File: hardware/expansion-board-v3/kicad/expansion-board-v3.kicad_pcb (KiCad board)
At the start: 6 copper layers, 100 x 62 mm, 156 parts, among them J1 PinHeader_2x20_P2.54mm_Vertic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, J2 U.FL_Hirose_U.FL-R-SMT-1_Vert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, J4 USB_C_Receptacle_HRO_TYPE-C-3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, J5 U.FL_Hirose_U.FL-R-SMT-1_Vert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, J6 U.FL_Hirose_U.FL-R-SMT-1_Vert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, J8 U.FL_Hirose_U.FL-R-SMT-1_Vert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, Q2 SOT-23, Q3 SOT-23, Q4 SOT-23, Q5 SOT-23, SW1 SolderJumper-2_P1.3mm_Open_Pa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, SW2 SolderJumper-2_P1.3mm_Open_Pa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, U1 SOT-23-5, U10 QFN-48-1EP_7x7mm_P0.5mm_EP5.1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, U11 DFN-8-1EP_2x2mm_P0.5mm_EP0.86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, U12 SOT-363_SC-70-6, U13 AD8319_LFCSP-8-EP, U14 MSOP-8_3x3mm_P0.65mm, U15 SOT-23-6, U16 SOT-363_SC-70-6, U17 SOT-363_SC-70-6, U2 SOT-23-5, U3 SOT-23-5, U4 BNO085_LGA-28, U5 BMP388_LGA-10, U6 LGA-16_3x3mm_P0.5mm, U7 ATGM336H_LCC-18, U8 QFN-56-1EP_7x7mm_P0.4mm_EP3.2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, U9 SOIC-8_5.3x5.3mm_P1.27mm, Y1 Crystal_SMD_3225-4Pin_3.2x2.5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, Y2 Crystal_SMD_3225-4Pin_3.2x2.5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, Y3 Crystal_SMD_3215-2Pin_3.2x1.5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

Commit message: fix(hw): D2/D3 补阴极标记线，版本号 V3.3 → V3.4
手工贴片前查极性时发现的最后一个坑：D2/D3 是 0402 封装的 ESD 管，KiCad 官方
封装 D_0402_1005Metric 只给了个**半径 0.05mm 的圆点**标 pin1，配 0.1mm 线宽，
实物可见直径约 0.2mm。这尺寸在放大镜下都难认，而它俩混在 22 个 0402 电容和
9 个 0402 电感中间外观几乎一样——贴反了电路直接不工作。

改成阴极侧一条 0.7mm 长、0.2mm 宽的标记线，比原来醒目一个数量级。
D1 是 SOD-123，官方封装的 [ 形阴极标记已经够大，不动。

方向是按电路复核过的，不是照搬 KiCad 的 pad1=阴极约定：
  D1  pad1=VCC_5V(K)/pad2=USB_VBUS(A)   USB 5V 经肖特基流向 VCC_5V，防倒灌 ✓
  D2  pad1=ANT1090_EXT(K)/pad2=GND(A)   ESD 阴极接信号、阳极接地 ✓
  D3  pad1=ANT_978(K)/pad2=GND(A)       同上 ✓

顺带删掉官方封装那个小圆点——它正好落在新标记线正中央，不删 silk_overlap
会从 1 涨到 3。挪开躲它也不行：0402 焊盘外侧就那么点地方，挪远了顶到别的
元件。删完 DRC 回到基线（未连通 0 / 铜层 0 / 丝印 2+1）。

## 修了一个更要命的隐患

排查副本重建失败时挖出来的：gen_pcb.py 读的 build/expansion.net.xml **没有
任何脚本负责刷新**，只有它读、没人写，全靠人记得手动导。实际那份停留在
11 天前，目录改名成 v3 后里面的封装库名还是旧的 "expansion-board-v3.1:"。

后果不是报错那么简单——KiCad 在库目录不存在时 FootprintLoad 返回 None，
抛的是 "NoneType object has no attribute FootprintLoad"，完全看不出根因是
网表陈旧。更坏的情况是网表只旧一点点（比如少个元件），那就会**静默**按
过时数据重建整块板。

现在 gen_pcb.py 会比对网表和原理图的 mtime，旧了就自动重导。

## 验证

  幂等          重复跑清 2 加 2，不叠加
  DRC           未连通 0 / 铜层 0 / 丝印与改动前完全一致
  从零重建       副本上 gen_pcb + gen_polarity_marks，标记坐标与主板逐个一致
  已进 rebuild.sh，重建不会丢

版本号按规则 +0.1：V3.3 的 Gerber 已经生成过，不升号会出现同一版本号对应
两份不同 Gerber。实物板仍是 V3.2，ASSEMBLY/CHECKLIST 里的首批板丝印错位
警告不受影响。
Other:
- board text added: "V3.4 2026-08"
- board text removed: "V3.3 2026-08"
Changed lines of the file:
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@@
 		(attr smd)
 		(duplicate_pad_numbers_are_jumpers no)
-		(fp_circle
-			(center -1.09 0)
-			(end -1.04 0)
-			(stroke
-				(width 0.1)
-				(type solid)
-			)
-			(fill no)
-			(layer "F.SilkS")
-		)
 		(fp_rect
 			(start -0.93 -0.47)
@@
 		(attr smd)
 		(duplicate_pad_numbers_are_jumpers no)
-		(fp_circle
-			(center -1.09 0)
-			(end -1.04 0)
-			(stroke
-				(width 0.1)
-				(type solid)
-			)
-			(fill no)
-			(layer "F.SilkS")
-		)
 		(fp_rect
 			(start -0.93 -0.47)
@@
 	)
 	(gr_line
+		(start 127.21 62.45)
+		(end 127.21 61.75)
+		(stroke
+			(width 0.2)
+			(type default)
+		)
+		(layer "F.SilkS")
+	)
+	(gr_line
+		(start 139.625 85.845)
+		(end 140.325 85.845)
+		(stroke
+			(width 0.2)
+			(type default)
+		)
+		(layer "F.SilkS")
+	)
+	(gr_line
 		(start 50 50)
 		(end 150 50)
@@
 		)
 	)
-	(gr_text "V3.3   2026-08"
+	(gr_text "V3.4   2026-08"
 		(at 100 80 0)
 		(layer "B.SilkS")

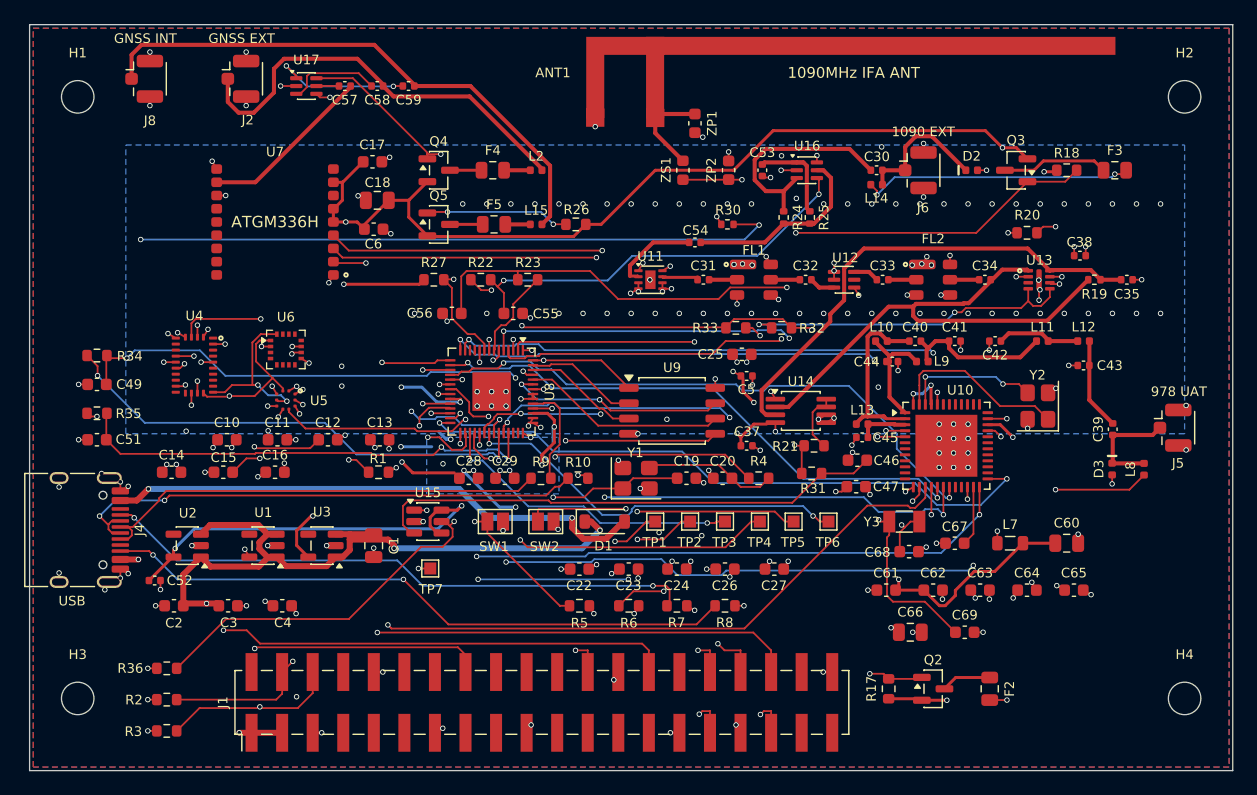
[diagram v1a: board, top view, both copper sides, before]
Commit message: fix(hw): IFA 馈线两侧挖无铜走廊，否则 0.15mm 线宽的前提不成立
0.15mm 是按**纯微带**算的（嘉立创 JLC06161H-3313 官方计算器 0.1509mm→50Ω，
参考面是 In1 完整地平面）。纯微带的前提是两侧没有近距离共面地，而板上 GND
铺铜的 zone clearance 只有 0.15mm——走线两侧 0.15mm 就是铜，实物是共面波导
不是微带，和设计模型不是一回事。天线那边刚因为「腿被 GND 包围」栽过一次。

走廊沿走线生成 keepout：半宽 = 半线宽 + 0.5mm，0.5mm ≈ 5 倍介质厚
（L1-L2 prepreg 3313 单张 0.0994mm），微带边缘场大约 3 倍介质厚内衰减完。
逐点扫描验证：两侧 ±0.20/0.35/0.50mm 命中铜 0 处，外侧 0.75mm 仍有铜
（只挖走廊没挖过头），ZP1.2 接地脚照常在铜里。

三个边界条件：
· **只挖 F.Cu**。In1 是这条微带的参考地平面，挖了不是更干净，是把传输线拆了
· **禁过孔**。只挡铺铜的话 route_rf 的 GND 缝合孔照样能打进来，一个 0.3mm
  接地过孔落在 50Ω 线旁 0.2mm 处比铺铜更糟——那是集中接地点，直接阻抗突变
· **不禁焊盘**。走廊两端压着 ZP1.1/ZS1.1 两个射频焊盘，禁了 DRC 立刻报违例

同时修 route_ifa_feed.py 一个自伤 bug：它删掉 ANT1090_IFA 的**所有**走线，
却只重布 ANT1→ZP1 一段，ZP1→ZS1 被删了没补（上一轮是拿 /tmp 里的临时脚本
手工补的，跑一次 run_route.sh 就又没了）。删多少补多少。

板子按固化后的布局从零重跑到第②"步：过孔全部重新放置（QFN 扇出环 + 60 栅栏
+ 183 缝合 + 35 EP 散热 = 313）。数字段走线仍为零，等 freerouting 指令。
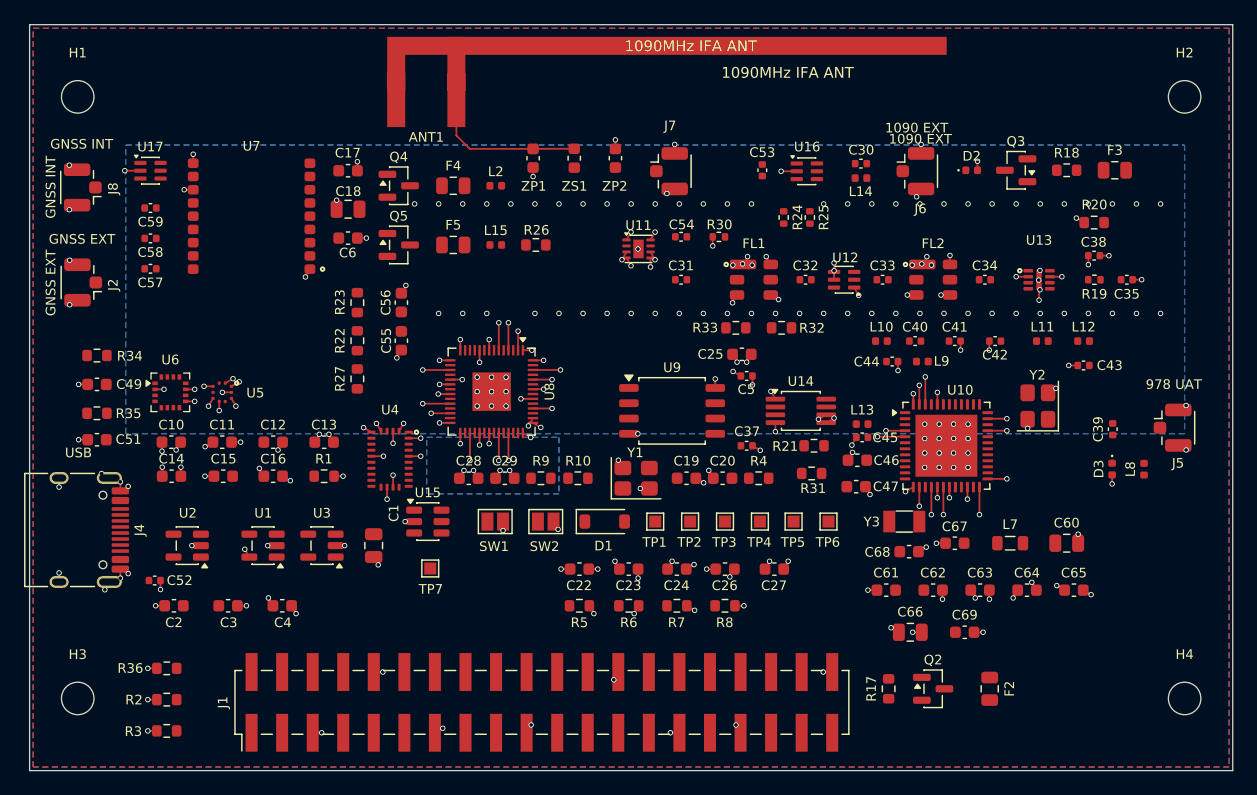
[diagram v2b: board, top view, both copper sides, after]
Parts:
- added J7: U.FL_Hirose_U.FL-R-SMT-1_Vertical, U.FL_Hirose_U.FL-R-SMT-1_Vertical, F.Cu at (103.6, 62.2)
- moved C59 23.7 mm to (60.0, 65.2), turned to 0 degrees
- moved C58 22.7 mm to (60.0, 67.8)
- moved C57 22.2 mm to (60.0, 70.3)
- moved J2 22.0 mm to (54.0, 71.4), turned to 180 degrees
- moved U4 18.0 mm to (80.0, 86.1)
- moved ANT1 16.5 mm to (85.5, 57.8)
- moved U17 14.7 mm to (60.0, 62.1)
- moved R23 14.3 mm to (77.2, 73.1), turned to -90 degrees
- moved ZP1 13.8 mm to (91.8, 61.1)
- moved R22 11.4 mm to (77.2, 76.3), turned to 90 degrees
- moved J8 10.9 mm to (54.0, 63.5), turned to 180 degrees
- moved R27 10.4 mm to (77.2, 79.4), turned to 90 degrees
- moved U6 10.2 mm to (61.7, 80.6)
- moved C55 9.57 mm to (80.9, 76.3), turned to -90 degrees
- moved ZP2 9.46 mm to (98.7, 61.1)
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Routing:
- net 3V3_GNSS: track 169.6 -> 0.00 mm, vias 6 -> 0
- net RF_DET_OUT: track 122.3 -> 0.00 mm, vias 6 -> 0
- net SUBG_MISO: track 78.2 -> 0.89 mm, vias 2 -> 1
- net VCC_5V: track 74.4 -> 0.00 mm, vias 4 -> 0
- net LEVEL_BIAS: track 72.1 -> 0.00 mm, vias 5 -> 0
- net GNSS_TXD: track 69.0 -> 0.00 mm, vias 2 -> 0
- net SLICER_LEVEL: track 66.5 -> 0.00 mm, vias 4 -> 0
- net SUBG_RESET: track 67.1 -> 2.48 mm, vias 4 -> 2
- net GNSS_PPS: track 63.4 -> 0.00 mm, vias 2 -> 0
- net SUBG_TMSC: track 63.7 -> 2.29 mm, vias 3 -> 1
- net GNSS_RXD: track 61.1 -> 0.00 mm, vias 2 -> 0
- net BIAS_EN_978: track 60.9 -> 0.00 mm, vias 3 -> 0
- net 3V3_RF: track 66.8 -> 6.25 mm, vias 16 -> 8
- net IMU_INT: track 60.4 -> 0.00 mm, vias 2 -> 0
- net BIAS_EN_1090: track 58.7 -> 2.29 mm, vias 2 -> 1
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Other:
- board text added: "V3.5 2026-08"
- board text removed: "3V3-D"
- board text removed: "3V3-G"
- board text removed: "3V3-RF"
- board text removed: "AD8313"
- board text removed: "AD8319"
- board text removed: "ATGM336H"
- board text removed: "BMP388"
- board text removed: "BNO085"
- board text removed: "CC1312R"
- board text removed: "LNA1"
- board text removed: "LNA2"
- board text removed: "QMC5883"
- board text removed: "RP2040"
- board text removed: "SW1090"
- board text removed: "SWGNSS"
- board text removed: "TLV3501"
- board text removed: "V3.4 2026-08"
- board text removed: "W25Q128"

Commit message: chore(hw): 按固化布局重建板子，J7 标注 + 无铜走廊 + 45° 扇出全部落盘
板子重跑到第②"步并补齐第⑦/⑦'步：309 走线 / 313 过孔（QFN 扇出环 + 60 栅栏
+ 183 缝合 + 35 EP 散热，全部重新放置）。板级文字 12 条无重复，'1090 IFA'
已在板上，位号字高 0.8mm。

DRC 只剩 via_dangling 35（数字段未布线，缝合孔暂时悬空，布通后自然消）
和 silk_edge_clearance 2（既存）。silk_overlap 归零。

数字段仍未布线：freerouting 卡在 45° 后处理不出 SES，四种组合全试过都一样，
见下一条提交里的记录。
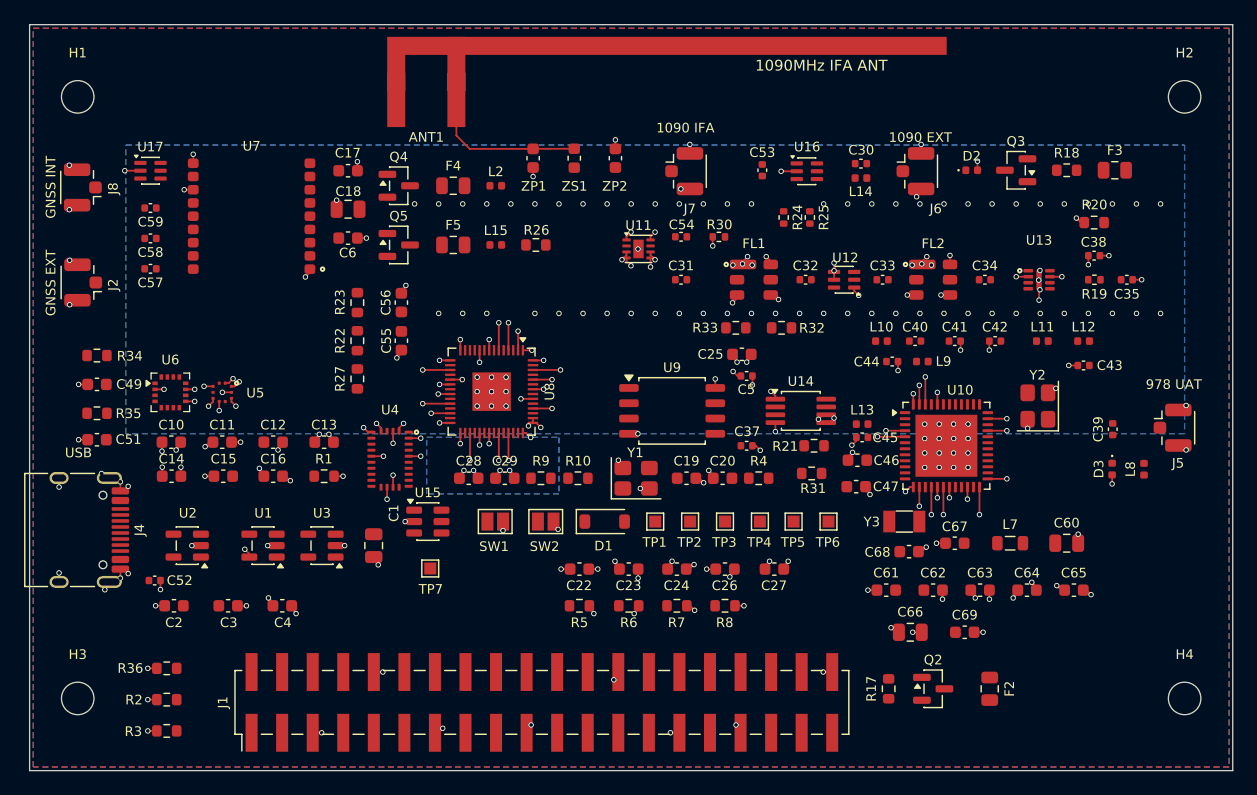
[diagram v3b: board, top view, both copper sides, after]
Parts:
- moved J7 1.26 mm to (104.9, 62.2)
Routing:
- net GND: track 100.6 -> 103.8 mm
- net 3V3_DIG: track 34.8 -> 35.9 mm
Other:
- board text added: "1090 IFA"

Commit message: feat(hw): 改用 KRT 布数字段，未连通 207 → 55
freerouting 布得完但吐不出 SES（六种组合全试过，见上一条提交）。换 KRT——
KiCadRoutingTools 0.19.1，Rust A*，装在 KiCad 10 的 3rdparty 插件目录里。
上一条记忆写着「KRT 已经找不回来了」，是错的，它一直在。

它直接读写 .kicad_pcb，不走 DSN/SES，freerouting 那个坑整个绕开；而且是
octilinear（H/V/45°），天然没有会卡死的 45 度化后处理。布线本体只花 17 秒。

结果：走线 309→1864（F.Cu 1688 / B.Cu 85 / In2.Cu 91），过孔 437，
真缺线 207→55。铜层 DRC 只剩 starved_thermal 2 + track_dangling 1。
射频 258 段全在 F.Cu、线宽 0.15、零过孔，In1 参考面完整；
IFA 馈线四段一字未动，无铜走廊仍在，馈线两侧和天线两脚 0 处命中铜。

## 四个坑，都踩了

1. **它不重新填充覆铜。** 新走线/过孔穿过旧的填充铜，DRC 报 clearance 505 +
   hole_clearance 200，看着像布线质量差。跑一次 ZONE_FILLER 之后 505→33、200→0
   ——而 Track↔Track 自始至终只有 4 条。判据：先看违例的参与者类型，带 Zone 的
   先去填铜再下结论。

2. **per-netclass 规则要显式给。** --clearance 一旦显式传就会覆盖它从 sibling
   .kicad_pro 自动读的 per-netclass 值。第一轮传了 0.15，POWER 类（要求 0.2、
   线宽 0.5）被按 Default 布成 0.15——93 条通但 33 条 clearance 违例，而且
   USB_VBUS/VCC_5V 用 0.15mm 载流根本不够。改用 --power-nets + --power-nets-widths
   之后 80 条通、clearance 归零。少通 13 条是真实代价，不是退步。

3. **reconciliation 阶段不看 --nets 过滤。** 我排除了全部 27 个 RF50 网络，
   它的 kicad-oracle reconnect 照着 KiCad DRC 的未连通表把 7 条射频布到了
   B.Cu/In2.Cu 上，打了 18 个过孔——那是在 50Ω 线的参考面上开洞。事后清掉，
   再迭代 clean_dangling 收敛。

4. **它会偷改 .kicad_pro**（这次 26 项），老毛病。在 build/krt/ 副本里跑，
   只回拷 .kicad_pcb。

另外它放了 3 个 0.25/0.15 的过孔（板规要求直径 ≥0.3、环宽 ≥0.07）。改 0.45 会撞
邻居，改 0.30/0.15 正好：直径等于下限、环宽 0.075>0.07，两项都过。

剩余 55 条真缺线里 3V3_GNSS 独占 14 条——它没有覆铜平面（可缝合网络只有
3V3_DIG/3V3_RF/GND/RP_1V1），却被我当平面网排除掉了，下一轮不该排除它。
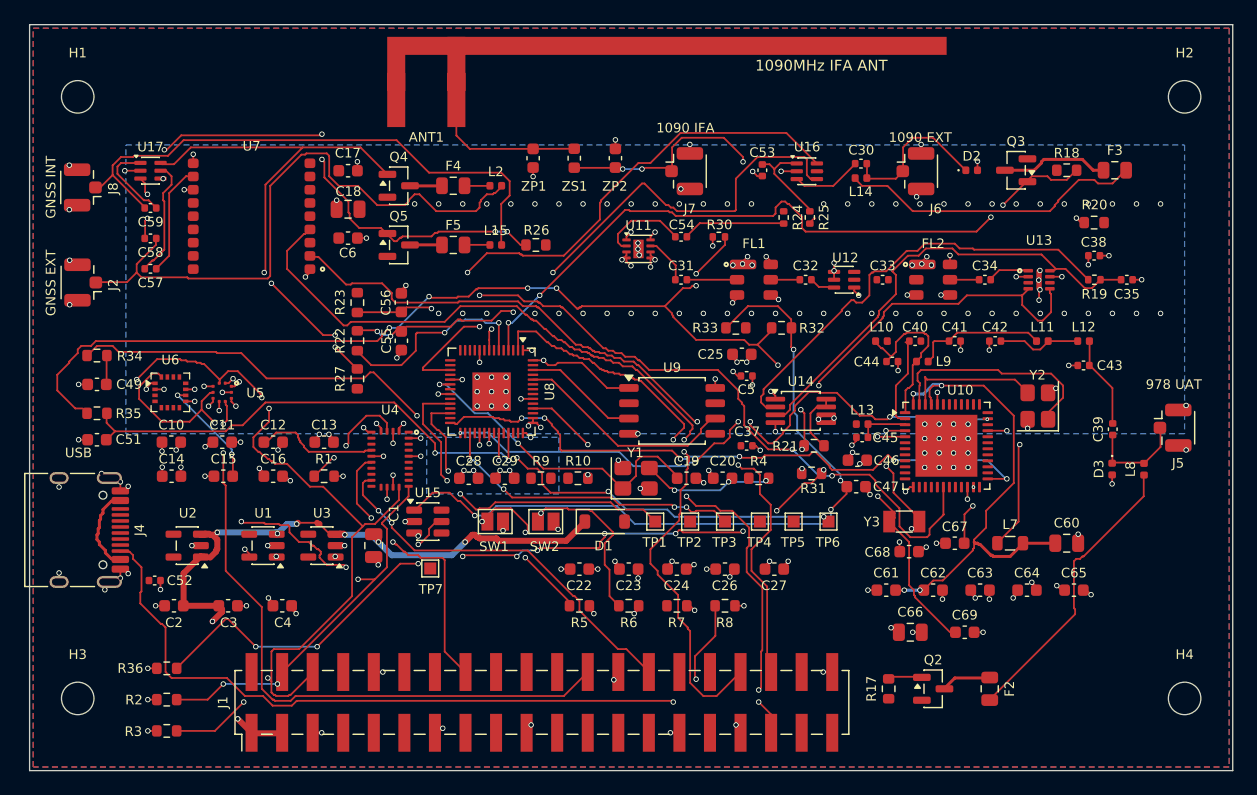
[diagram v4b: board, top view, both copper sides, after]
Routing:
- net RF_DET_OUT: track 0.00 -> 119.3 mm, vias 0 -> 11
- net GNSS_PPS: track 0.00 -> 74.6 mm, vias 0 -> 2
- net I2C_SCL: track 0.00 -> 69.8 mm, vias 0 -> 6
- net I2C_SDA: track 0.00 -> 66.6 mm, vias 0 -> 6
- net VCC_5V: track 0.00 -> 66.5 mm, vias 0 -> 10
- net USB_CC2: track 0.00 -> 65.4 mm, vias 0 -> 2
- net GNSS_TXD: track 0.00 -> 63.6 mm, vias 0 -> 2
- net SLICER_LEVEL: track 0.00 -> 62.9 mm, vias 0 -> 4
- net SUBG_IRQ: track 4.58 -> 64.0 mm, vias 2 -> 4
- net BIAS_EN_1090: track 2.29 -> 58.4 mm, vias 1 -> 4
- net BARO_INT: track 0.00 -> 53.9 mm, vias 0 -> 2
- net ANT_GNSS_EXT: track 0.00 -> 51.5 mm
- net SUBG_TCKC: track 2.48 -> 52.9 mm, vias 2 -> 6
- net ANT_SEL_GNSS_A: track 0.89 -> 50.7 mm, vias 1 -> 7
- net ANT_SEL_1090_V1: track 0.00 -> 49.3 mm, vias 0 -> 4
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
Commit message: feat(hw): KRT 收尾脚本化，真缺线 55 → 41（3V3_GNSS 那 14 条清零）
上一轮把 3V3_GNSS 当"平面网"排除掉了，可它**根本没有覆铜平面**——板上真有
覆铜的只有 GND / 3V3_DIG / 3V3_RF / RP_1V1。它需要走线连接却被挡在门外，
55 条真缺线里一家独占 14 条。这一轮放开，14 条清零。

根治办法不是把名单改对，是**不再写死名单**：krt_post.py 的 nets 模式直接从板上
的覆铜区读，板子怎么变名单就怎么变。POWER/POWER_LO 的线宽同样从 .kicad_pro 的
netclass 读，并自动跳过已有平面和已布好的射频。

新增 tools/krt_post.py，把 KRT 的收尾固化成一条命令（手工来一遍必漏）：

    ① 清射频越层  —— 它的 reconciliation 阶段不看 --nets 过滤，会照着 KiCad DRC
                     的未连通表把射频布到 B.Cu/In2.Cu 并打过孔，那是在 50Ω 线的
                     参考面上开洞
    ② 修不合规过孔 —— 实测它放过 0.25/0.15；改 0.45 会撞邻居，0.30/0.15 正好
                     （直径等于下限、环宽 0.075>0.07）
    ③ 覆铜重填    —— 它不填。不填的话新走线穿过旧填充铜，DRC 报 clearance 505 +
                     hole_clearance 200，看着像布线烂，其实全是 Track/Via↔Zone
    ④ 断头铜迭代  —— 删过孔会露出新的断头走线，一轮清不完，清到收敛为止

本轮结果：走线 1997 段（F.Cu 1806 / B.Cu 94 / In2.Cu 97），过孔 451，
真缺线 41 处 / 31 网络，铜层 DRC 3 条（starved_thermal 2 + track_dangling 1）。
射频 257 段全在 F.Cu、线宽 0.15、零过孔；IFA 馈线 4 段完好，走廊仍禁铺铜禁过孔，
馈线两侧和天线两脚 0 处命中铜；板级文字 12 条无重复。

剩下 41 条分散在 31 个网络（QSPI/SUBG/USB 各 1-5 条），已是硬骨头，
再压要靠 rip-up reroute 或改布局。
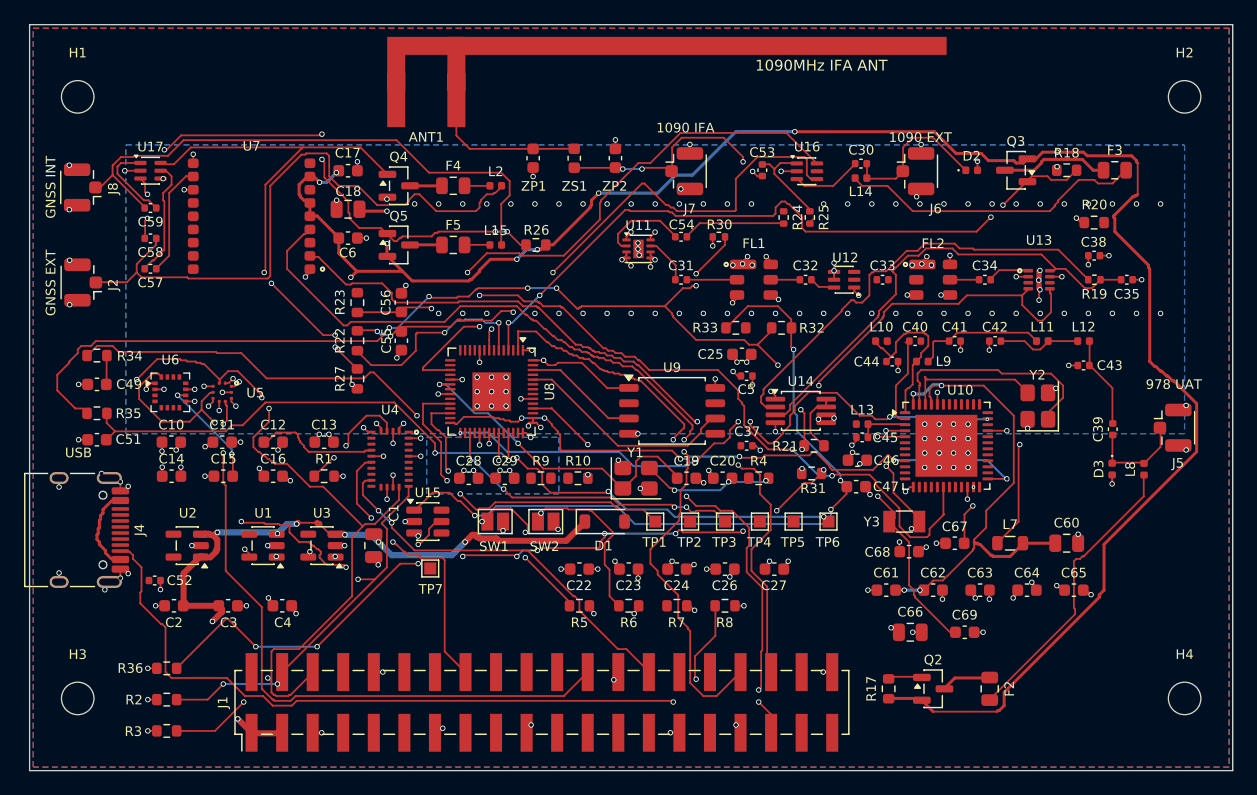
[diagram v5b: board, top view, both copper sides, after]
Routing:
- net 3V3_GNSS: track 0.00 -> 190.7 mm, vias 0 -> 14
